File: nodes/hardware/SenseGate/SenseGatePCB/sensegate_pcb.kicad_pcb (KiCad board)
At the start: 2 copper layers, 64.6 x 110 mm, 42 parts, among them J1 Conn_01x12_Pin, J2 Conn_01x12_Pin, J3 Conn_01x02_Socket, J4 Conn_01x24_Pin, J5 Conn_01x04_Socket, J6 Conn_01x04_Socket, J7 Conn_01x04_Socket, J8 Conn_01x04_Socket, J9 Conn_01x04_Socket, Q1 AO3401A, Q5 SS8050, SW5 SW_DPDT_x2, U1 DD05CVSA, U2 mt3608_dcdc_converter

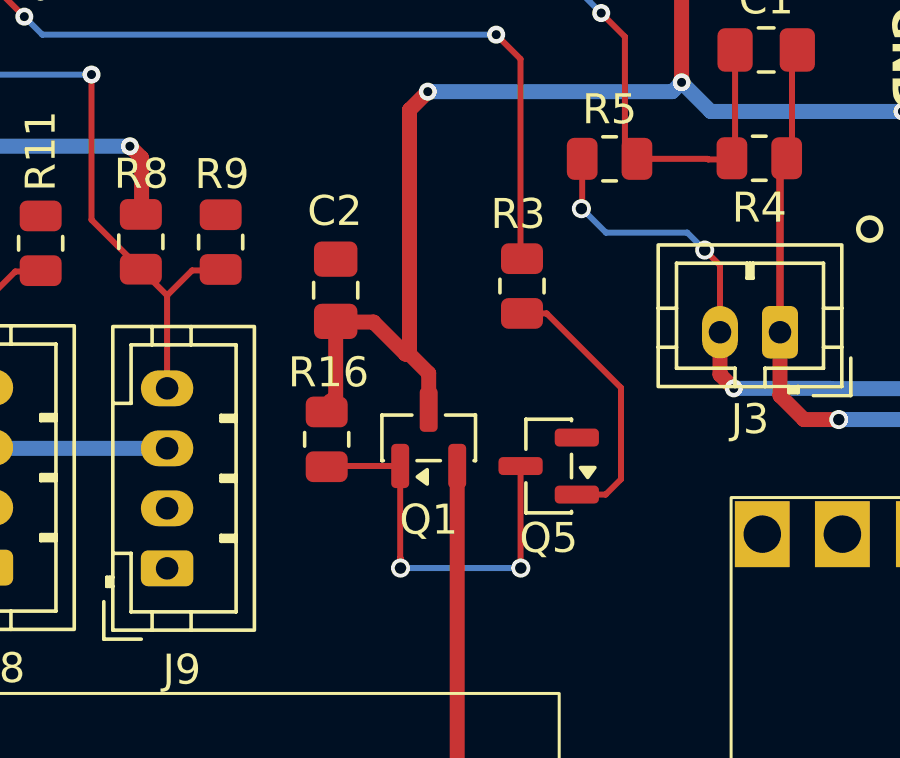
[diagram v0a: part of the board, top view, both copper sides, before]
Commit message: figuring out mosfet useage
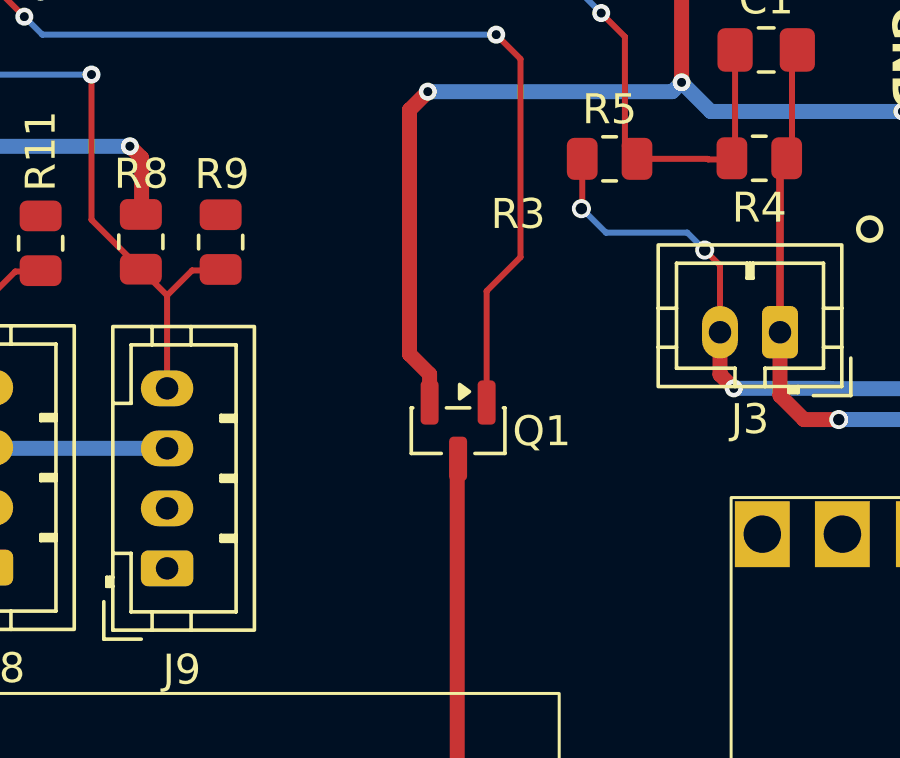
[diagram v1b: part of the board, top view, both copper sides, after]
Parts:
- removed C2: C, Capacitor_SMD:C_0805_2012Metric_Pad1.18x1.45mm_HandSolder
- removed Q5: SS8050, Package_TO_SOT_SMD:SOT-23
- removed R16, R3: R, Resistor_SMD:R_0805_2012Metric
- moved Q1 1.01 mm to (133.6, 107.9), turned to -90 degrees
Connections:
- Q1 pad 1: Net-(Q1-G) -> TOG_20V
- Q1 pad 2: Net-(Q1-S) -> VBAT
- Q1 pad 3: VBAT -> Net-(Q1-D)
- U2 pad 3: Net-(Q1-S) -> Net-(Q1-D)
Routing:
- net Net-(Q1-G): track 13.3 -> 0.00 mm, vias 2 -> 0
- net Net-(Q1-S): track 12.5 -> 0.00 mm
- net Net-(Q1-D): track 0.00 -> 12.5 mm
- net Net-(Q5-B): track 9.06 -> 0.00 mm
- net VBAT: track 133.5 -> 127.7 mm
- net TOG_20V: track 82.4 -> 87.7 mm

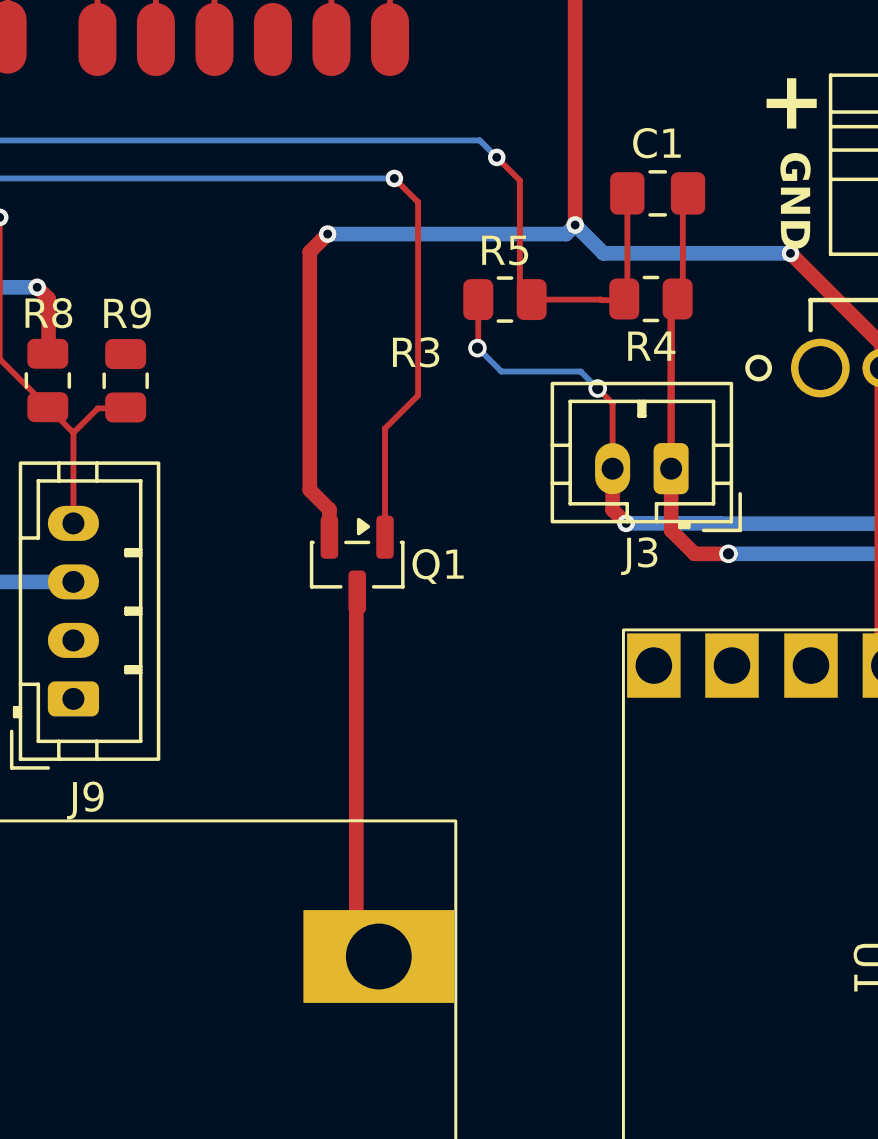
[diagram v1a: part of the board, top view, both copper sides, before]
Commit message: added description for resistor values
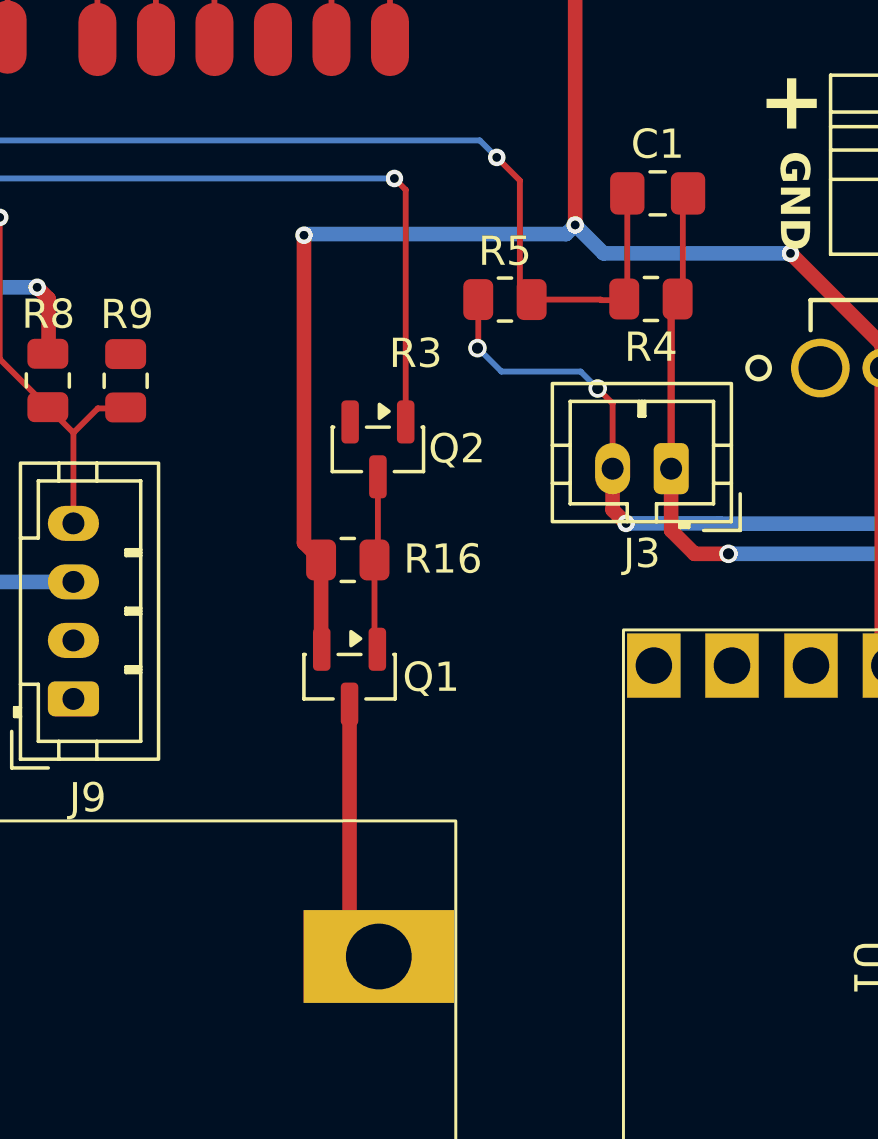
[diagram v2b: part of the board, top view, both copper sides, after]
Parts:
- added Q2: BSS138, Package_TO_SOT_SMD:SOT-23, F.Cu at (134.3, 104.0)
- added R16: R, Resistor_SMD:R_0805_2012Metric, F.Cu at (133.2, 107.8)
- moved Q1 3.84 mm to (133.3, 111.8)
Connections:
- Q1 pad 1: TOG_20V -> Net-(Q1-G)
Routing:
- net Net-(Q1-G): track 0.00 -> 5.98 mm
- net TOG_20V: track 87.7 -> 83.1 mm
- net VBAT: track 127.7 -> 132.0 mm
- net Net-(Q1-D): track 12.5 -> 9.04 mm

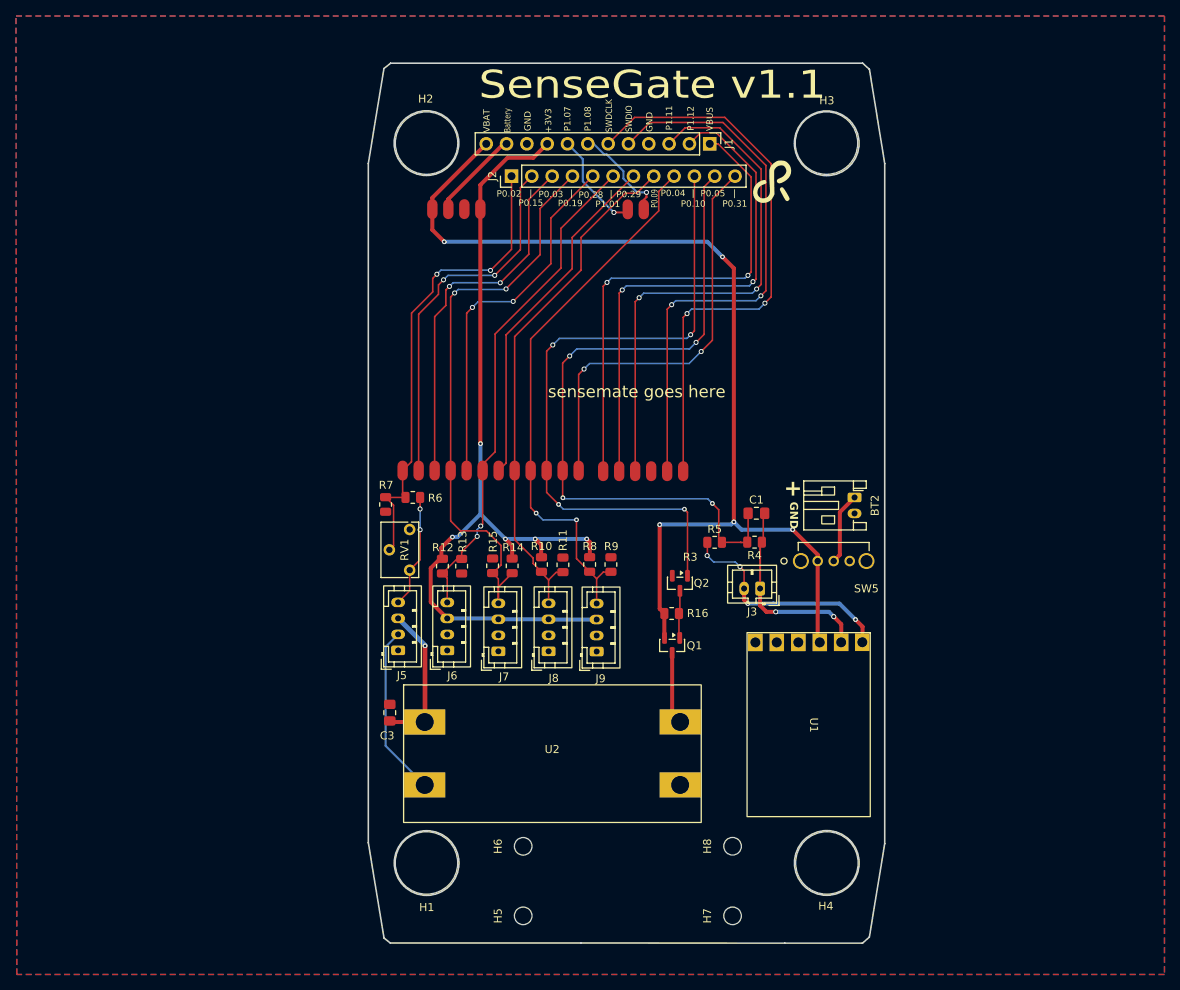
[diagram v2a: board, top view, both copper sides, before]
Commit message: added hole to access mate reset pin, optimized power swtich placement and generated new gerber files
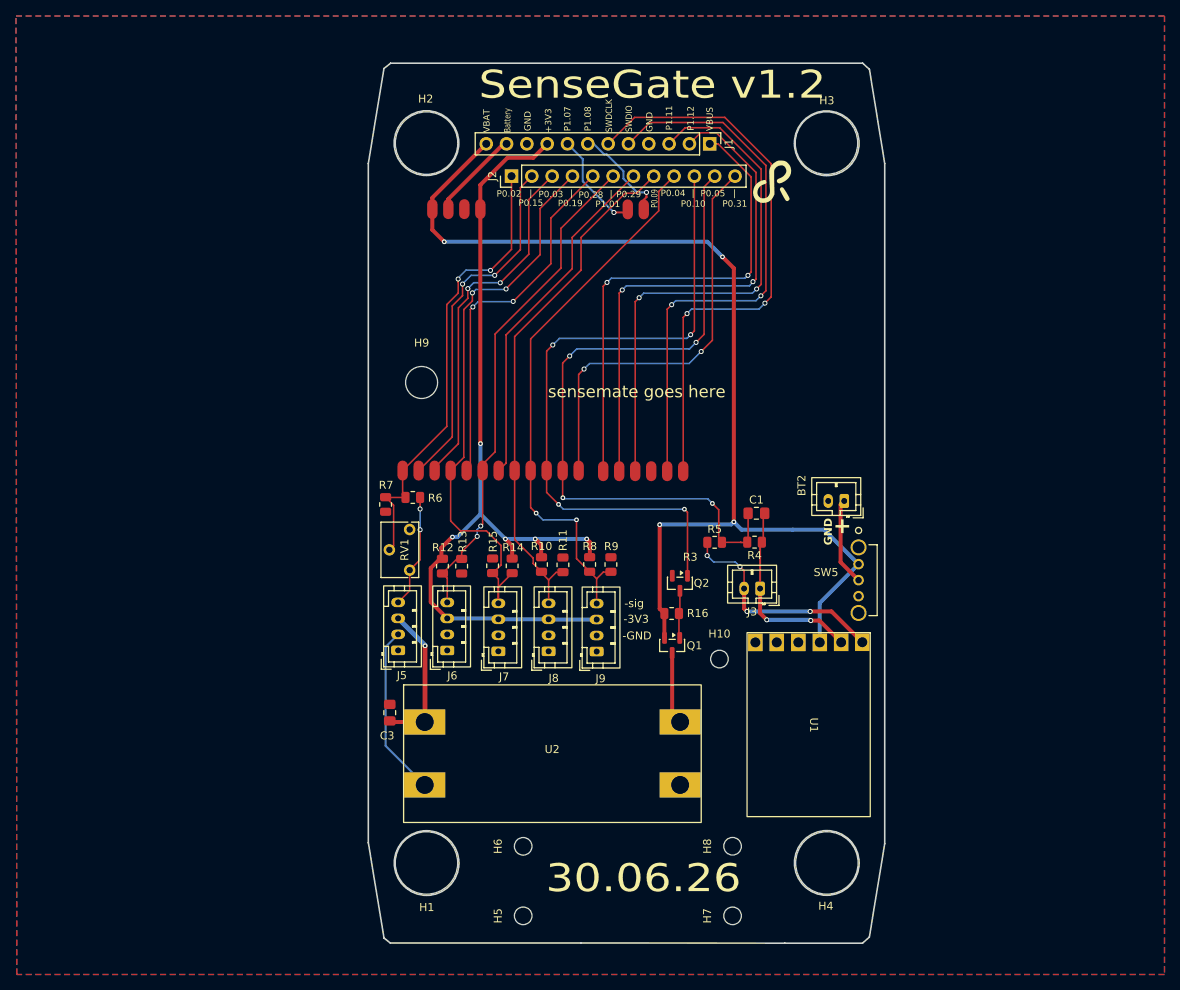
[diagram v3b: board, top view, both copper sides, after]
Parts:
- added H10: MountingHole, MountingHole:MountingHole_2.2mm_M2, F.Cu at (139.2, 113.5)
- added H9: MountingHole, MountingHole:MountingHole_4mm, F.Cu at (102.0, 78.9)
- BT2: footprint Connector_JST:JST_PH_S2B-PH-K_1x02_P2.00mm_Horizontal -> Connector_JST:JST_PH_B2B-PH-K_1x02_P2.00mm_Vertical
- moved SW5 5.12 mm to (156.6, 101.6), turned to -90 degrees
- moved BT2 1.36 mm to (154.8, 93.7), turned to 180 degrees
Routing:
- net VBAT: track 132.0 -> 138.3 mm, vias 5 -> 4
- net Net-(BT2-+): track 9.03 -> 11.0 mm
- net IS_ADC: track 59.3 -> 57.5 mm
- net Net-(J2-Pin_2): track 46.1 -> 44.4 mm
- net Net-(J2-Pin_3): track 46.3 -> 44.8 mm
- net reed_sw_03_measure: track 72.9 -> 71.6 mm
- net Net-(J3-Pin_1): track 25.1 -> 24.4 mm
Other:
- board text added: "-3V3"
- board text added: "-GND"
- board text added: "-sig"
- board text added: "30.06.26"
- board text added: "SenseGate v1.2"
- board text removed: "SenseGate v1.1"
